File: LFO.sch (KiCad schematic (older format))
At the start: 16 parts, among them Q3 2N3904, U5 TL072, U6 TL074

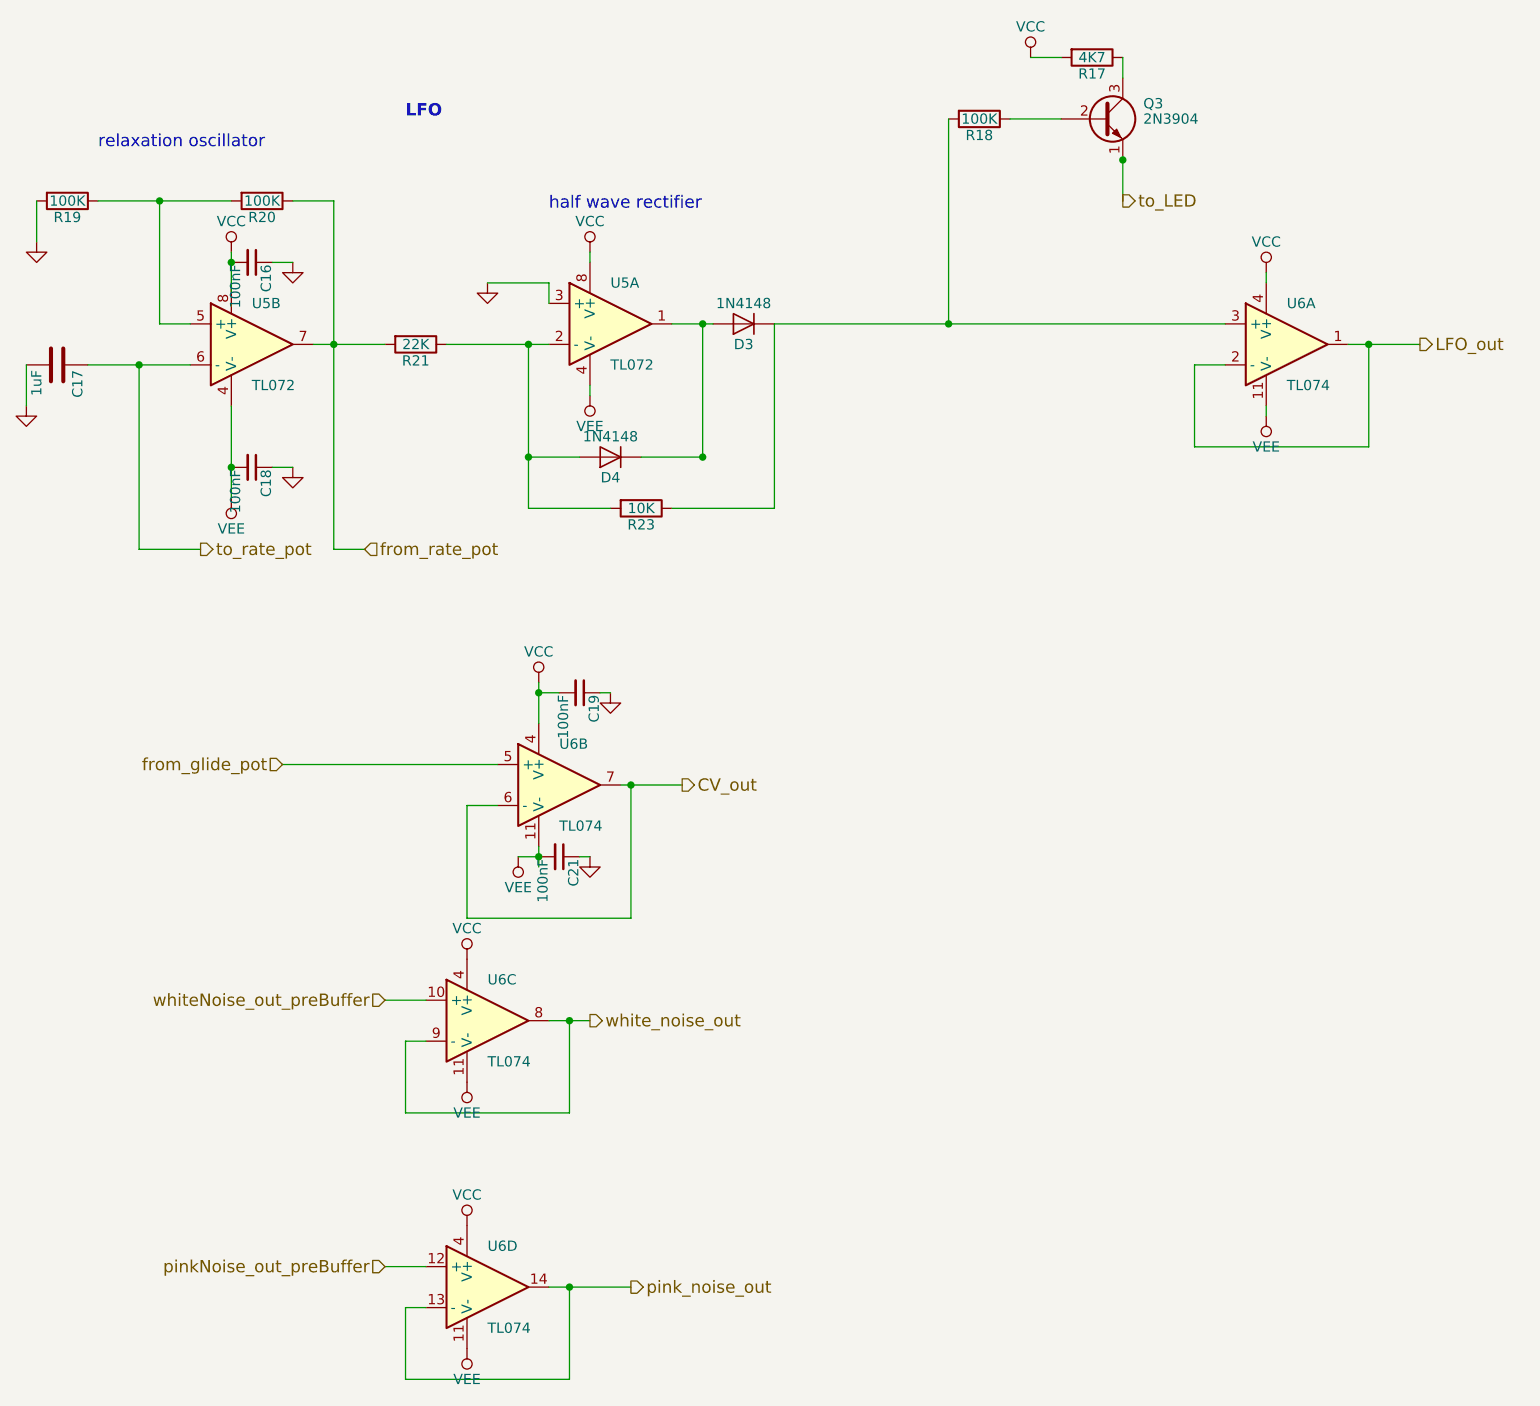
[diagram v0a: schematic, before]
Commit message: changed to 40106 osc and one shot, but input schmitt not working
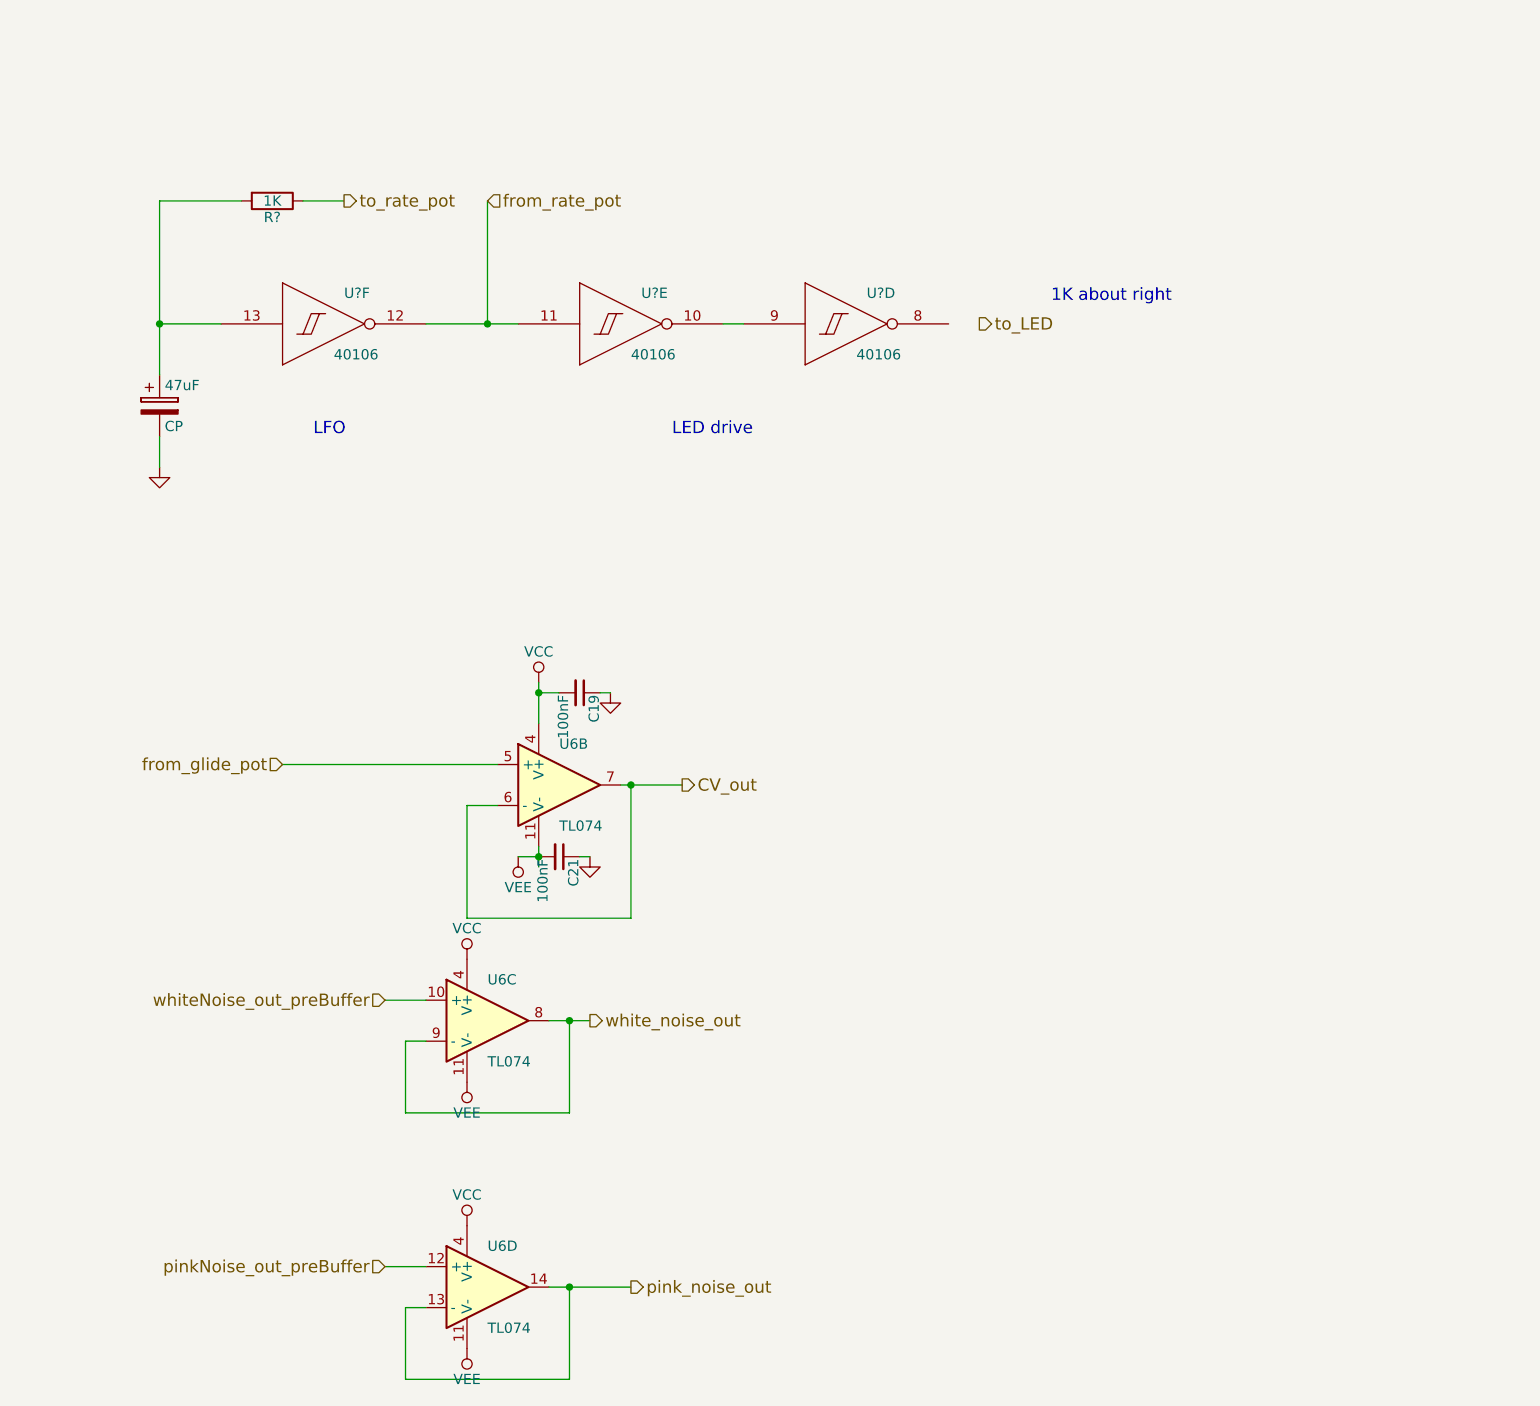
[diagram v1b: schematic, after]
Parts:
- removed C16, C18: 100nF, Capacitors_THT:C_Disc_D3.0mm_W2.0mm_P2.50mm, symbol C_Small
- removed C17: 1uF, Capacitors_THT:C_Rect_L7.2mm_W5.5mm_P5.00mm_FKS2_FKP2_MKS2_MKP2, symbol C
- removed D3, D4: 1N4148, Diodes_THT:D_DO-41_SOD81_P7.62mm_Horizontal, symbol D
- removed Q3: 2N3904, TO_SOT_Packages_THT:TO-92_Molded_Narrow, symbol 2N3904
- removed R17: 4K7, Resistors_THT:R_Axial_DIN0204_L3.6mm_D1.6mm_P7.62mm_Horizontal, symbol R
- removed R18, R19, R20: 100K, Resistors_THT:R_Axial_DIN0204_L3.6mm_D1.6mm_P7.62mm_Horizontal, symbol R
- removed R21: 22K, Resistors_THT:R_Axial_DIN0204_L3.6mm_D1.6mm_P7.62mm_Horizontal, symbol R
- removed R23: 10K, Resistors_THT:R_Axial_DIN0204_L3.6mm_D1.6mm_P7.62mm_Horizontal, symbol R
- removed U5: TL072, Housings_DIP:DIP-8_W7.62mm_LongPads, symbol TL072
- removed unit 1 of U6
- added 47uF: CP, symbol CP
- added R?: 1K, Resistors_THT:R_Axial_DIN0204_L3.6mm_D1.6mm_P7.62mm_Horizontal, symbol R
- added U? (x3): 40106, symbol 40106
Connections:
- net GND: now also 47uF.2
- net from_rate_pot: now also U?.11 (In), U?.12 (Out)
- net to_rate_pot: now also R?.1
- new net: 47uF.1, R?.2, U?.13 (In)
- new net: U?.10 (Out), U?.9 (In)
- new net VDD: U?.14 (VDD), U?.14 (VDD), U?.14 (VDD)
- new net VSS: U?.7 (VSS), U?.7 (VSS), U?.7 (VSS)
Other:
- note added: "1K about right"
- note added: "LED drive"
- note removed: "half wave rectifier"
- note removed: "relaxation oscillator"
